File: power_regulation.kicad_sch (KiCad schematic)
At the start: 117 parts, among them IC3 MIE1W0505BGLVH-3R-P, J10 Conn_01x02_Pin, J11 Conn_01x02_Pin, J12 Conn_01x02_Pin, J9 V_bat_secondary, U10 TPS7A2055PDBVR, U11 TLV75733PDYDR, U12 OPA2387DR, U13 TPS7A2050PDBVR, U14 TPS7A2033PDBVR, U15 TPS7A2033PDBVR, U16 TPS7A2050PDBVR, U17 TPS7A2018PDBVRG4, U18 TPS7A2050PDBVR, U19 TPS7A2045PDBVR, U6 TPS62933, U7 TPS62933, U8 MCP1502T-50E/CHY, U9 NCV8114BSN330T1G

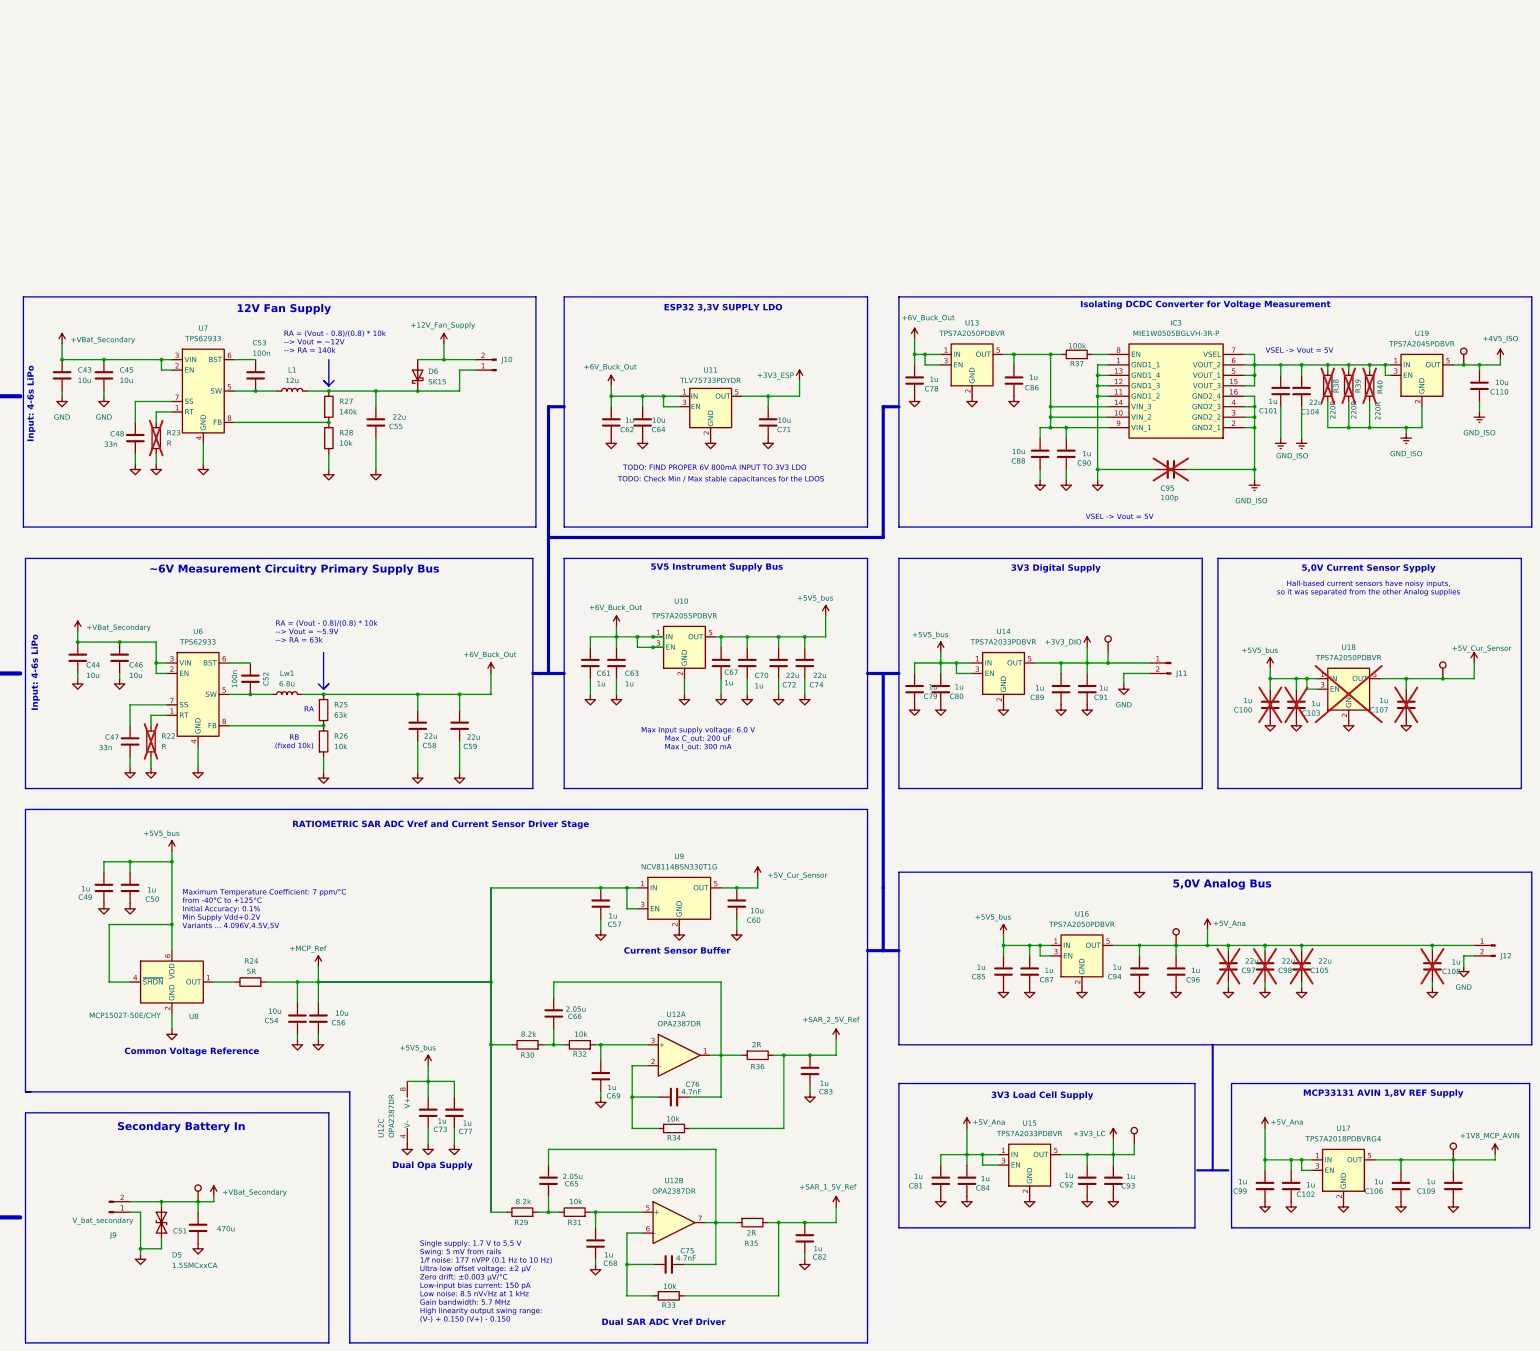
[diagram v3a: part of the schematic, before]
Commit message: Improved NTC measurements, improved layout. Added proper startup sequence for the power stages.
[KiCad Version: 10.0.4]
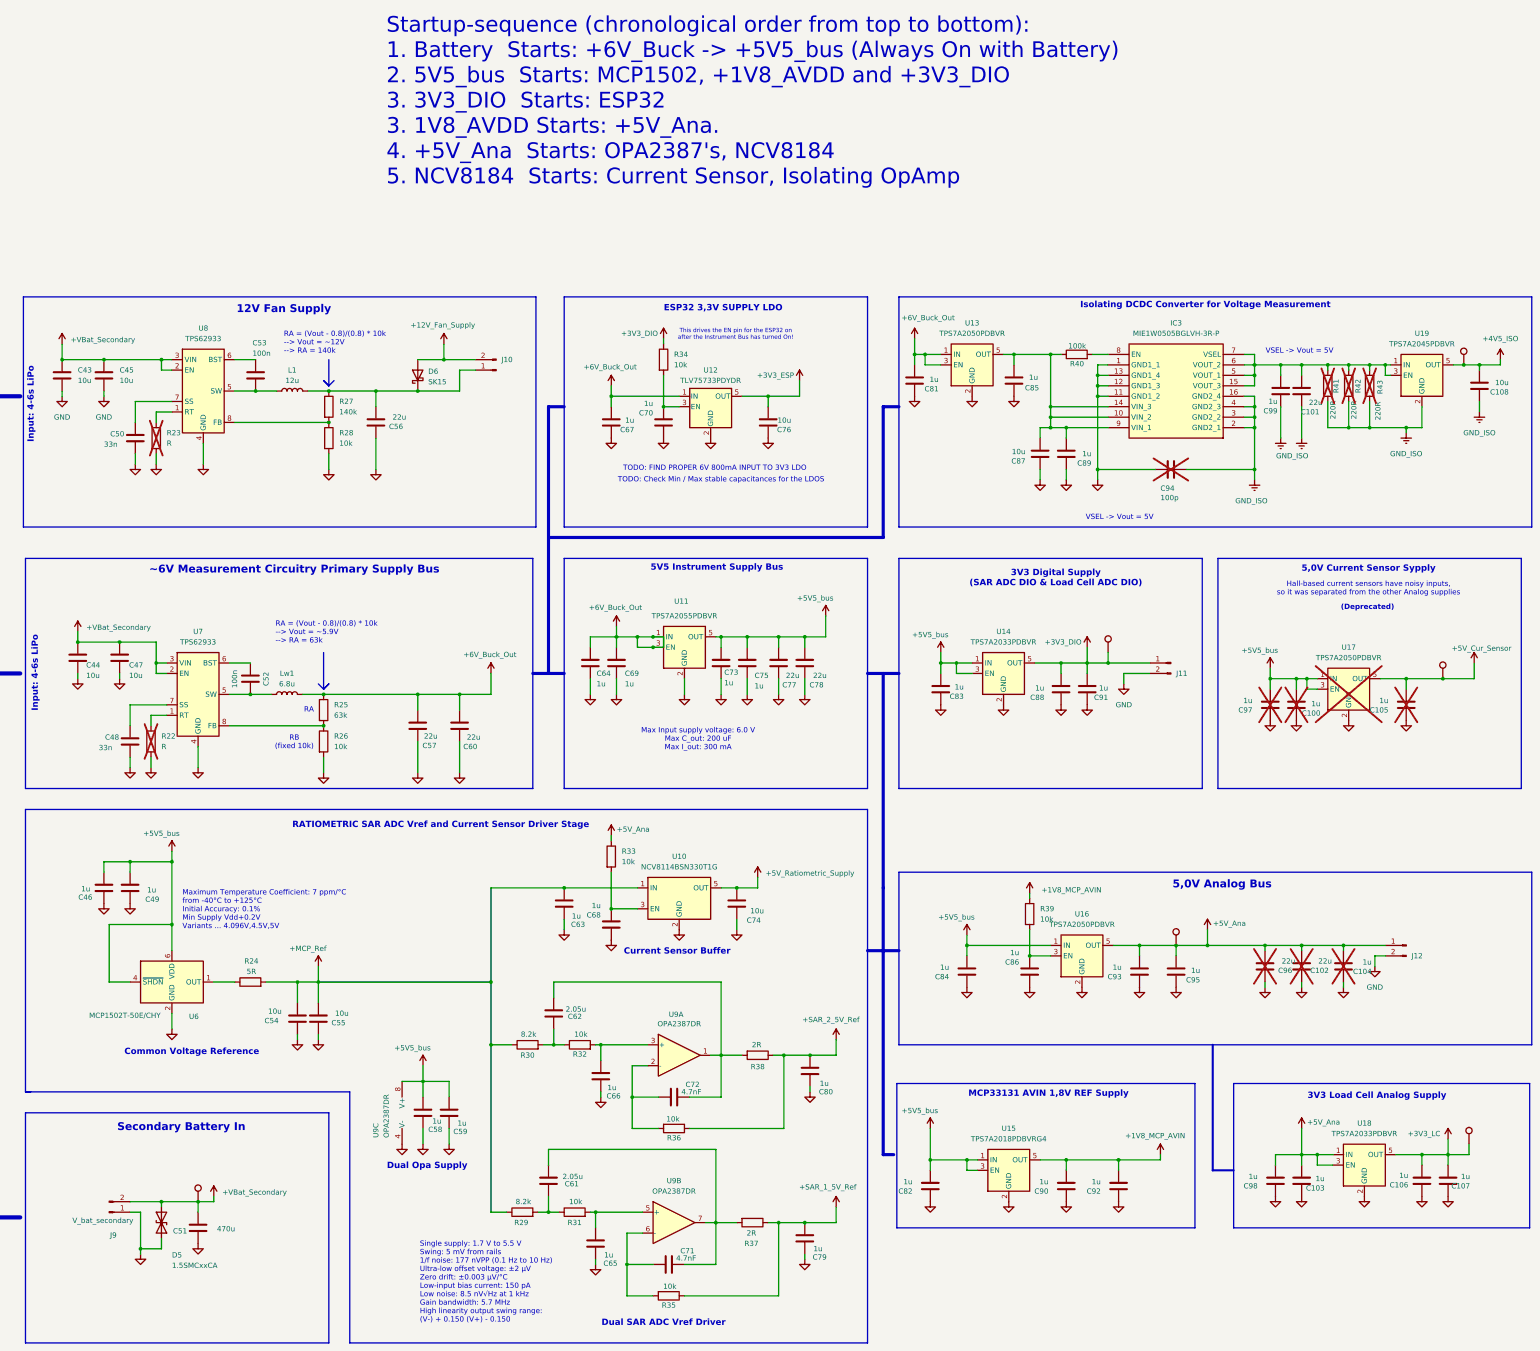
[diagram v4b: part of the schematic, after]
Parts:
- removed AVIN1: TestPoint, TestPoint:TestPoint_Pad_D1.0mm, symbol Connector:TestPoint
- removed C102, C80, C87: 1u, Capacitor_SMD:C_0603_1608Metric_Pad1.08x0.95mm_HandSolder, symbol Device:C
- removed C64: 10u, Capacitor_SMD:C_0603_1608Metric_Pad1.08x0.95mm_HandSolder, symbol Device:C
- removed C97: 22u, Capacitor_SMD:C_1206_3216Metric_Pad1.33x1.80mm_HandSolder, symbol Device:C
- added C68, C70, C86: 1u, Capacitor_SMD:C_0603_1608Metric_Pad1.08x0.95mm_HandSolder, symbol Device:C
- added R33, R34, R39: 10k, Resistor_SMD:R_0603_1608Metric_Pad0.98x0.95mm_HandSolder, symbol Device:R
- renumbered C103 to C100, C104 to C101, C105 to C102, C84 to C103, C108 to C104, C107 to C105, C92 to C106, C93 to C107, C110 to C108, C49 to C46, C46 to C47, C47 to C48, C50 to C49, C48 to C50, C56 to C55, C55 to C56, C58 to C57, C73 to C58, C77 to C59, C59 to C60, C65 to C61, C66 to C62, C57 to C63, C61 to C64, C68 to C65, C69 to C66, C62 to C67, C63 to C69, C75 to C71, C76 to C72, C67 to C73, C60 to C74, C70 to C75, C71 to C76, C72 to C77, C74 to C78, C82 to C79, C83 to C80, C78 to C81, C99 to C82, C79 to C83, C85 to C84, C86 to C85, C88 to C87, C89 to C88, C90 to C89, C106 to C90, C109 to C92, C94 to C93, C95 to C94, C96 to C95, C98 to C96, C100 to C97, C81 to C98, C101 to C99, R33 to R35, R34 to R36, R35 to R37, R36 to R38, R37 to R40, R38 to R41, R39 to R42, R40 to R43, U9 to U10, U10 to U11, U11 to U12, U17 to U15, U18 to U17, U15 to U18, U8 to U6, U6 to U7, U7 to U8, U12 to U9
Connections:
- net +1V8_MCP_AVIN: now also R39.1
- net +3V3_DIO: now also R34.1
- net +5V5_bus: now also C82.2, U15.1 (IN), U15.3 (EN); no longer U16.3 (EN)
- net +5V_Ana: now also R33.1; no longer C82.2, U15.1 (IN), U15.3 (EN)
- net +5V_Cur_Sensor: no longer C74.2, U10.5 (OUT)
- net +6V_Buck_Out: no longer U12.3 (EN)
- net +MCP_Ref: no longer U10.3 (EN)
- net GND: now also C68.1, C70.1, C86.1
- new net: C86.2, R39.2, U16.3 (EN)
- new net: C70.2, R34.2, U12.3 (EN)
- new net: C68.2, R33.2, U10.3 (EN)
- new net +5V_Ratiometric_Supply: C74.2, U10.5 (OUT)
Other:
- note added: "(Deprecated)"
- note added: "3V3 Digital Supply (SAR ADC DIO & Load Cell ADC DIO)"
- note added: "3V3 Load Cell Analog Supply"
- note added: "Startup-sequence (chronological order from top to bottom): 1. Battery Starts: +6V_Buck -> +5V5_bus (Always On with Battery) 2. 5V5_bus Starts: MCP1502, +1V8_AVDD and +3V3_DIO 3. 3V3_DIO Starts: ESP32 3. 1V8_AVDD Starts: +5V_Ana. 4. +5V_Ana Starts: OPA2387's, NCV8184 5. NCV8184 Starts: Current Sensor, Isolating OpAmp"
- note added: "This drives the EN pin for the ESP32 on after the Instrument Bus has turned On!"
- note removed: "3V3 Digital Supply"
- note removed: "3V3 Load Cell Supply"
- moved on the sheet: C103, C104, C106, C107, C58, C59, C63, C82, C83, C84, C90, C92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

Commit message: Add Shutdown Protection Diodes between Power Stages
[KiCad Version: 10.0.4]
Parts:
- removed Vref2: TestPoint, TestPoint:TestPoint_Pad_D1.0mm, symbol Connector:TestPoint
- added D? (x2): CDBU40-HF, Diode_SMD:D_0603_1608Metric, symbol Diode:CDBU40-HF
- renumbered Vref3 to Vref2
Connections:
- net +1V8_MCP_AVIN: now also D?.2 (A)
- net +5V5_bus: now also D?.1 (K), D?.1 (K)
- net +5V_Ana: now also D?.2 (A)
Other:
- note added: "Safety Diodes Keeps the ADC Supplies at Higher voltage level than the Analog input side on Shutdown."
- moved on the sheet: C102, C104, C84, C86, C93, C95, C96, J12, R39, U16

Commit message: Add Kelvin voltage measurement.
[KiCad Version: 10.0.4]
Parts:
- gave numbers to parts that had none: 2
- renumbered C99 to C100, C104 to C101, C100 to C102, C101 to C103, C103 to C104, C95 to C94, C94 to C95, C102 to C97, C97 to C98, C98 to C99

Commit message: Minor Tweaks.
[KiCad Version: 10.0.4]
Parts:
- renumbered C99 to C100, C100 to C101, C101 to C102, C102 to C103, C103 to C104, C104 to C105, C105 to C106, C106 to C107, C107 to C108, C108 to C109, C43 to C44, C44 to C45, C45 to C46, C46 to C47, C47 to C48, C48 to C49, C49 to C50, C50 to C51, C51 to C52, C52 to C53, C53 to C54, C54 to C55, C55 to C56, C56 to C57, C57 to C58, C58 to C59, C59 to C60, C60 to C61, C61 to C62, C62 to C63, C63 to C64, C64 to C65, C65 to C66, C66 to C67, C67 to C68, C68 to C69, C69 to C70, C70 to C71, C71 to C72, C72 to C73, C73 to C74, C74 to C75, C75 to C76, C76 to C77, C77 to C78, C78 to C79, C79 to C80, C80 to C81, C81 to C82, C82 to C83, C83 to C84, C84 to C85, C85 to C86, C86 to C87, C87 to C88, C88 to C89, C89 to C90, C90 to C91, C91 to C92, C92 to C93, C93 to C94, C94 to C95, C95 to C96, C96 to C97, C97 to C98, C98 to C99

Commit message: Add Secondary battery voltage measurement. Minor tweaks.
[KiCad Version: 10.0.4]
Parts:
- removed U10: NCV8114BSN330T1G, Package_SO:SOIC-8_3.9x4.9mm_P1.27mm, symbol Regulator_Linear:NCV8114BSN330T1G
- added C67: 1u, Capacitor_SMD:C_0603_1608Metric_Pad1.08x0.95mm_HandSolder, symbol Device:C
- added C84: 10u, Capacitor_SMD:C_0603_1608Metric_Pad1.08x0.95mm_HandSolder, symbol Device:C
- added IC3: NCV8184DR2G, SOIC127P600X175-8N, symbol SamacSys_Parts:NCV8184DR2G
- renumbered C97 to C100, C98 to C101, C99 to C102, C100 to C103, C101 to C104, C102 to C105, C103 to C106, C104 to C107, C105 to C108, C106 to C109, C107 to C110, C108 to C111, C109 to C112, C69 to C45, C44 to C46, C45 to C47, C46 to C48, C47 to C49, C48 to C50, C49 to C51, C50 to C52, C51 to C53, C52 to C54, C53 to C55, C54 to C56, C55 to C57, C56 to C58, C57 to C59, C58 to C60, C59 to C61, C60 to C62, C61 to C63, C62 to C65, C63 to C66, C65 to C68, C66 to C69, C67 to C70, C68 to C71, C70 to C72, C71 to C73, C72 to C74, C73 to C75, C74 to C76, C76 to C77, C77 to C78, C78 to C79, C79 to C80, C80 to C81, C75 to C82, C81 to C83, C82 to C85, C83 to C86, C84 to C87, C85 to C88, C86 to C89, C87 to C90, C88 to C91, C89 to C92, C90 to C93, C91 to C94, C92 to C95, C93 to C96, C94 to C97, C95 to C98, C96 to C99, IC3 to IC4, R33 to R24, R22 to R25, R23 to R26, R24 to R27, R25 to R28, R26 to R29, R27 to R30, R28 to R31, R29 to R32, R30 to R33, R31 to R34, R32 to R35, R34 to R36, R35 to R37, R36 to R38, R37 to R39, R38 to R40, R39 to R41, R40 to R42, R41 to R43, R42 to R44, R43 to R45, U11 to U10, U12 to U11, U13 to U12, U14 to U13, U15 to U14, U16 to U15, U17 to U16, U18 to U17, U19 to U18
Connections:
- net +5V5_bus: now also C67.2, IC3.8 (VIN)
- net +5V_Ratiometric_Supply: now also C84.2, IC3.1 (VOUT), IC3.4 (ADJ)
- net +MCP_Ref: now also IC3.5 (VREF/ENABLE)
- net GND: now also C67.1, C84.1, IC3.2 (GND_1), IC3.3 (GND_2), IC3.6 (GND_3), IC3.7 (GND_4)
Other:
- moved on the sheet: C45, C64, C82, R24
